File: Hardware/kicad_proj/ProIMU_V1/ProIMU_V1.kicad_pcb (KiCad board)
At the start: 2 copper layers, 50 x 50 mm, 72 parts, among them IC1 MP2731GQC-0000-Z, J1 Conn_01x04, J4 502570-0893, Q1 2SC4213, U1 ADM101E, U2 TJA1051T-3, U3 LTC2942-1, U4 AIR602, U5 BMP280, U6 MPU-9250, U7 TPS54308, U8 TPS54308, U9 STM32F412CEU6

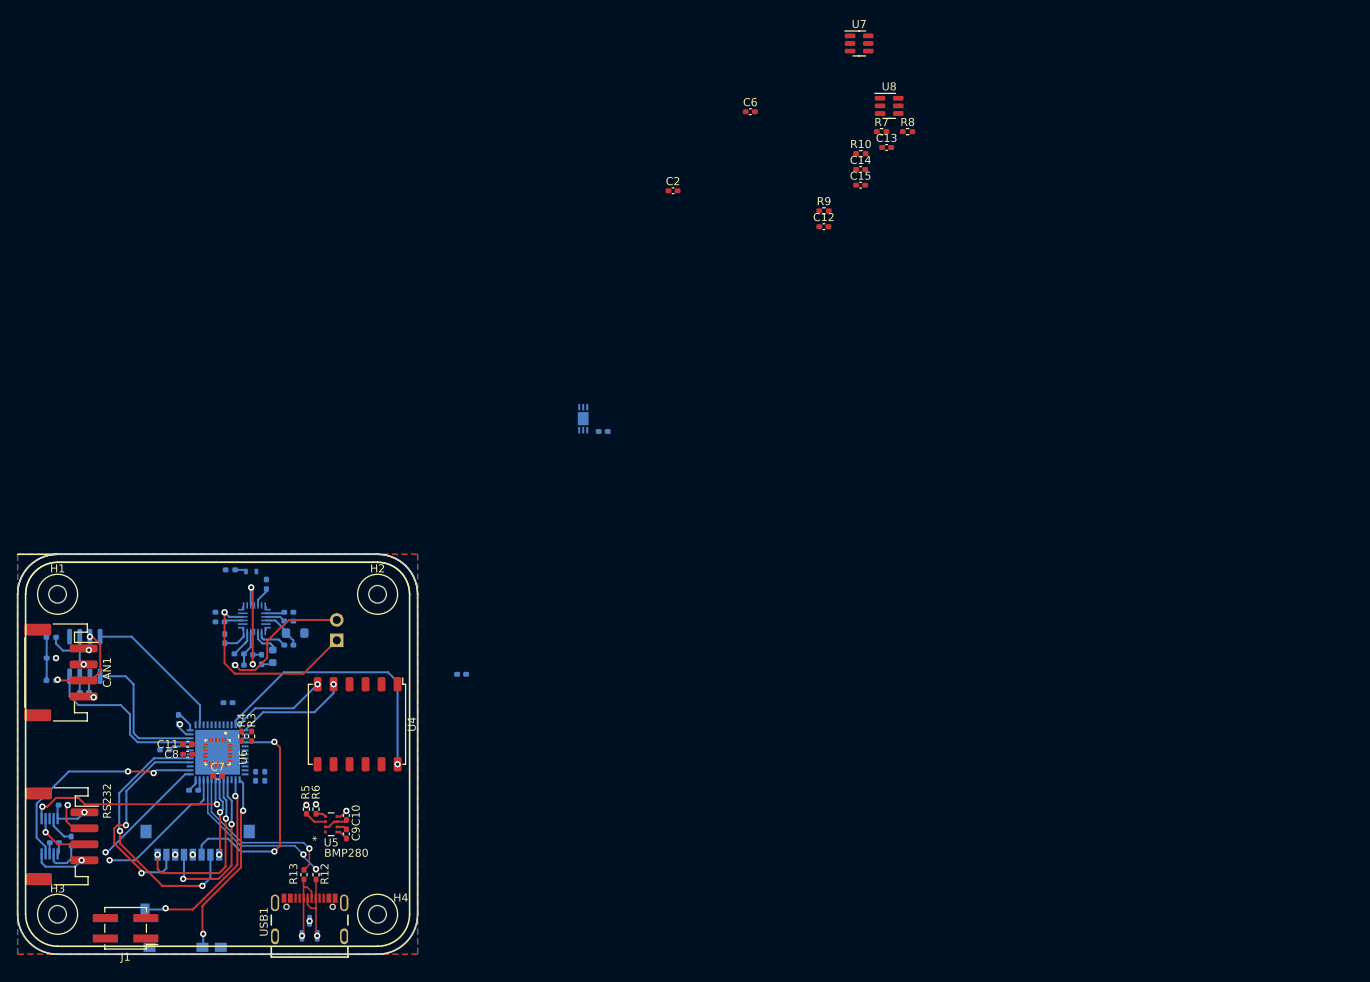
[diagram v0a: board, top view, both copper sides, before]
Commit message: Updated schematic, layout and footprints
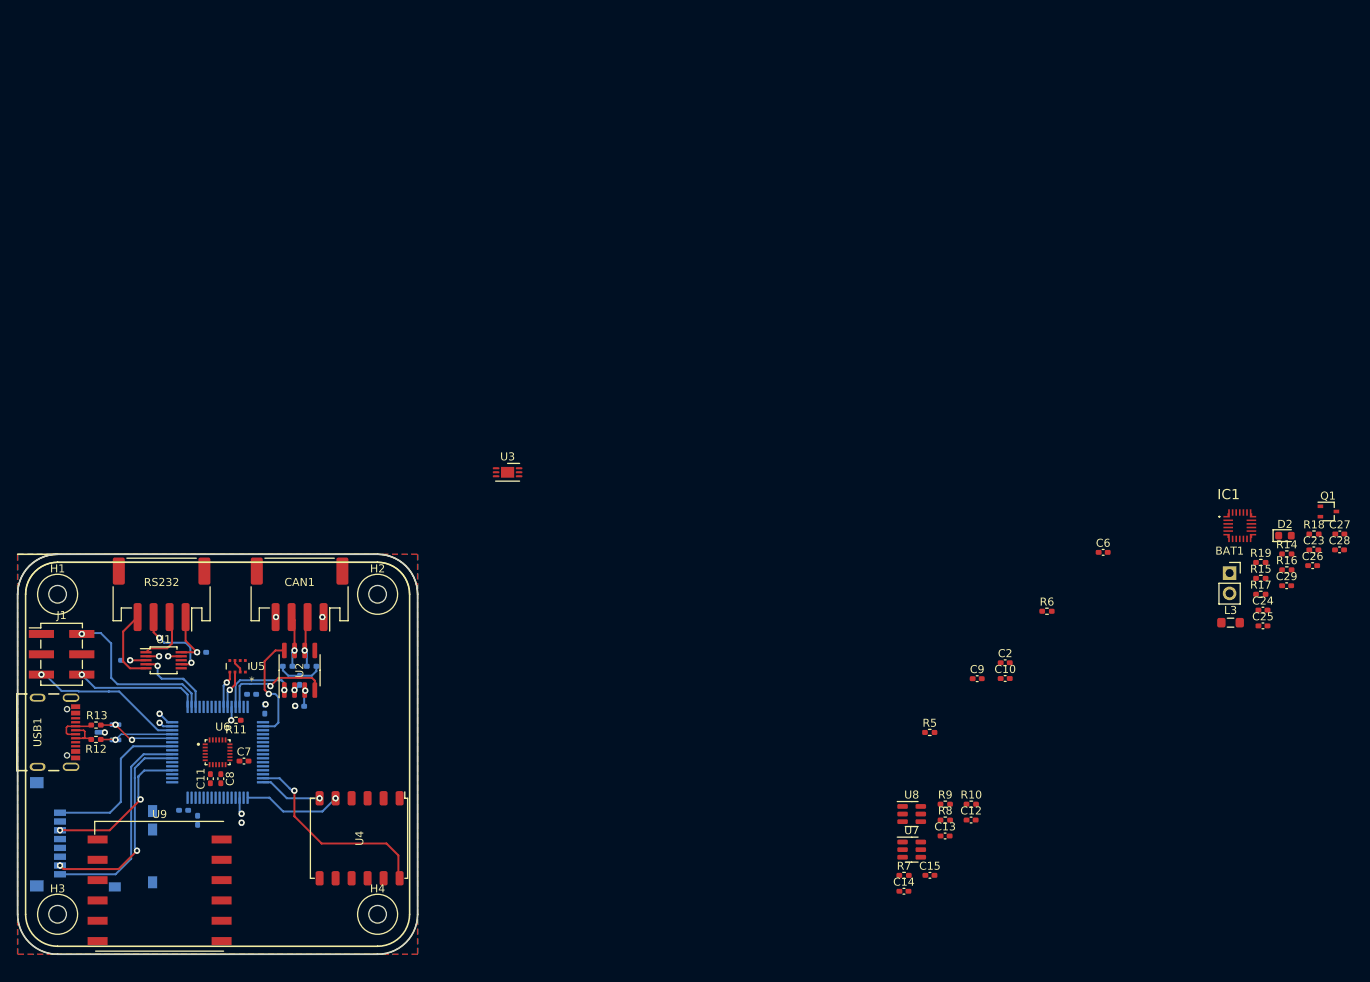
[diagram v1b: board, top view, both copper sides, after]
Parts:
- removed R3, R4: 2.2K, Resistor_SMD:R_0402_1005Metric_Pad0.72x0.64mm_HandSolder
- added U10: STM32F412RETx, Package_QFP:LQFP-64_10x10mm_P0.5mm, B.Cu at (148.5, 105.0)
- BAT1, C23, C24, C25, C26, C27, C28, C29, D2, IC1, L3, Q1, R11, R14, R15, R16, R17, R18, R19, U1, U2, U3: moved to F.Cu
- J1: value Conn_01x04 -> Conn_02x03_Counter_Clockwise; footprint Connector_PinHeader_2.54mm:PinHeader_2x02_P2.54mm_Vertical_SMD -> Connector_PinHeader_2.54mm:PinHeader_2x03_P2.54mm_Vertical_SMD
- U9: value STM32F412CEU6 -> L80-R; footprint footprints:QFN50P700X700X60-49N -> RF_GPS:Quectel_L80-R; moved to F.Cu
- moved C26 136.7 mm to (285.4, 81.7), turned to 0 degrees
- moved R18 135.2 mm to (285.6, 77.7), turned to 0 degrees
- moved Q1 134.9 mm to (287.4, 74.9), turned to 0 degrees
- moved R16 132.1 mm to (282.1, 82.2)
- moved C28 131.9 mm to (288.7, 79.7)
- moved C27 131.8 mm to (288.8, 77.7)
- moved C25 130.4 mm to (279.2, 89.2), turned to 0 degrees
- moved C24 129.8 mm to (279.2, 87.2), turned to 0 degrees
- moved C23 128.4 mm to (285.5, 79.7)
- moved R15 128.2 mm to (278.9, 83.3)
- moved R14 127.6 mm to (282.1, 80.2), turned to 0 degrees
- moved D2 127.4 mm to (281.9, 77.9), turned to 0 degrees
- moved R19 126.6 mm to (278.9, 81.3), turned to 0 degrees
- moved R17 125.2 mm to (278.9, 85.2), turned to 0 degrees
- moved IC1 123.7 mm to (276.3, 76.7), turned to 0 degrees
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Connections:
- net /SCK renamed /MCU/BMP280_I2C1_SDA
- net /SDA renamed /MCU/BMP280_I2C1_SCL
- D1 pad 1: /D1+ -> /Battery/D+
- D1 pad 2: /D1- -> /Battery/D-
- J1 pad 1: /MCU/SWDIO -> /MCU/DEBUG_UART1_RX
- J1 pad 2: /MCU/SWCLK -> /MCU/DEBUG_UART1_TX
- J1 pad 3: /MCU/MCU_RESET -> /MCU/NRST
- J4 pad 1: /MCU/SDCARD_D2 -> /MCU/SDCARD_SDIO_D2
- J4 pad 2: /MCU/SDCARD_D3 -> /MCU/SDCARD_SDIO_D3
- J4 pad 3: /MCU/SDCARD_CMD -> /MCU/SDCARD_SDIO_CLK
- J4 pad 5: /MCU/SDCARD_CLK -> /MCU/SDCARD_SDIO_CMD
- J4 pad 7: /MCU/SDCARD_DO -> /MCU/SDCARD_SDIO_D0
- J4 pad 8: /MCU/SDCARD_D1 -> /MCU/SDCARD_SDIO_D1
- R11 pad 2: Net-(R11-Pad2) -> Net-(U10-Pad60)
- R12 pad 1: /D1+ -> Net-(USB1-PadA6)
- R13 pad 2: /D1- -> Net-(USB1-PadA7)
- U1 pad 4: /MCU/RS232_RX -> /MCU/RS232_UART3_TX
- U1 pad 6: /MCU/RS232_TX -> /MCU/RS232_UART3_RX
- U2 pad 1: /MCU/CAN_TX -> /MCU/CAN1_TX
- U2 pad 4: /MCU/CAN_RX -> /MCU/CAN1_RX
- U4 pad 5: /MCU/WIFI_UART2_TX -> /MCU/WIFI_UART2_RX
- U4 pad 6: /MCU/WIFI_UART2_RX -> /MCU/WIFI_UART2_TX
- U6 pad 12: /MCU/MPU9250_INT -> /MCU/MPU9250_INT_EXTI4
- U6 pad 22: +3V3 -> /MCU/MPU9250_SPI1_nCSS
- U6 pad 23: /MPU9250_SDA -> /MCU/MPU9250_SPI1_SCK
- U6 pad 24: /MPU9250_SCK -> /MCU/MPU9250_SPI1_MISO
- U6 pad 9: unconnected-(U6-Pad9) -> /MCU/MPU9250_SPI1_MOSI
- U9 pad 1: +BATT -> unconnected-(U9-Pad1)
- U9 pad 10: /MCU/MPU9250_INT -> unconnected-(U9-Pad10)
- U9 pad 11: /MCU/WIFI_RESET -> unconnected-(U9-Pad11)
- U9 pad 12: /MCU/WIFI_UART2_RX -> Net-(U9-Pad12)
- U9 pad 2: /MCU/CAN_SHUTDOWN -> unconnected-(U9-Pad2)
- U9 pad 3: unconnected-(U9-Pad3) -> Net-(U9-Pad12)
- U9 pad 7: /MCU/MCU_RESET -> unconnected-(U9-Pad7)
- U9 pad 8: GND -> unconnected-(U9-Pad8)
- U9 pad 9: +3V3 -> unconnected-(U9-Pad9)
- USB1 pad A6: /D1+ -> Net-(USB1-PadA6)
- USB1 pad A7: /D1- -> Net-(USB1-PadA7)
- USB1 pad B6: /D1+ -> Net-(USB1-PadA6)
- USB1 pad B7: /D1- -> Net-(USB1-PadA7)
- USB1 pad S1: Earth -> unconnected-(USB1-PadS1)
- USB1 pad S2: Earth -> unconnected-(USB1-PadS2)
- USB1 pad S3: Earth -> unconnected-(USB1-PadS3)
- USB1 pad S4: Earth -> unconnected-(USB1-PadS4)
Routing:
- net /MCU/SDCARD_D3: track 33.8 -> 0.00 mm, vias 2 -> 0
- net /MCU/SDCARD_CMD: track 29.3 -> 0.00 mm, vias 2 -> 0
- net /MCU/RS232_RX: track 27.8 -> 0.00 mm, vias 2 -> 0
- net /MCU/SDCARD_DO: track 27.5 -> 0.00 mm, vias 2 -> 0
- net /MCU/RS232_TX: track 27.3 -> 0.00 mm, vias 2 -> 0
- net /MCU/SDCARD_SDIO_D1: track 0.00 -> 27.0 mm
- net /MCU/SDCARD_SDIO_D0: track 0.00 -> 26.4 mm, vias 0 -> 2
- net Net-(BAT1-Pad1): track 25.2 -> 0.00 mm, vias 1 -> 0
- net /MCU/SDCARD_DET_LEVEL: track 24.8 -> 0.00 mm, vias 2 -> 0
- net /MCU/SDCARD_DET_SWT: track 23.3 -> 0.00 mm, vias 2 -> 0
- net /MCU/SDCARD_D1: track 21.9 -> 0.00 mm, vias 2 -> 0
- net /MCU/CAN_RX: track 21.4 -> 0.00 mm
- net /MCU/DEBUG_UART1_TX: track 0.00 -> 21.1 mm, vias 0 -> 1
- net /MCU/SDCARD_CLK: track 20.8 -> 0.00 mm, vias 2 -> 0
- net /MCU/SDCARD_SDIO_D2: track 0.00 -> 20.6 mm
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
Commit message: Updated Layout
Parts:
- BAT1, C2, C23, C24, C25, C26, C27, C28, C29, D2, IC1, L3, Q1, R14, R15, R16, R17, R18, R19, U3: moved to B.Cu
- moved Q1 149.2 mm to (156.9, 147.3)
- moved C28 143.4 mm to (159.4, 141.6), turned to -90 degrees
- moved R16 143.3 mm to (154.6, 147.5), turned to 90 degrees
- moved C27 142.0 mm to (162.3, 142.2), turned to -90 degrees
- moved R18 141.3 mm to (157.4, 137.1)
- moved C26 141.1 mm to (156.5, 139.1), turned to -90 degrees
- moved D2 139.9 mm to (157.2, 141.3), turned to 180 degrees
- moved BAT1 138.6 mm to (148.7, 139.7)
- moved C29 138.6 mm to (154.6, 138.4)
- moved C23 137.2 mm to (163.4, 142.2), turned to -90 degrees
- moved R19 136.3 mm to (157.9, 143.9), turned to 180 degrees
- moved R17 135.8 mm to (156.2, 143.3), turned to -90 degrees
- moved R15 135.5 mm to (154.6, 137.1)
- moved C25 133.1 mm to (159.9, 148.1)
- moved IC1 130.0 mm to (161.9, 138.4), turned to 90 degrees
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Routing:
- net VDD: track 0.00 -> 10.0 mm, vias 0 -> 1
- net Net-(BAT1-Pad1): track 0.00 -> 8.39 mm, vias 0 -> 2
- net GND: track 3.61 -> 9.29 mm, vias 8 -> 18
- net Net-(IC1-Pad11): track 0.00 -> 5.40 mm
- net Net-(BAT1-Pad2): track 0.00 -> 5.32 mm, vias 0 -> 1
- net Net-(D2-Pad1): track 0.00 -> 4.03 mm
- net Net-(IC1-Pad22): track 0.00 -> 3.65 mm, vias 0 -> 1
- net Net-(C28-Pad1): track 0.00 -> 2.69 mm
- net Net-(IC1-Pad12): track 0.00 -> 2.42 mm
- net Net-(C28-Pad2): track 0.00 -> 2.37 mm
- net Net-(IC1-Pad24): track 0.00 -> 2.27 mm
- net /Battery/SYSTEM_OUT: track 0.00 -> 2.04 mm
- net Net-(C24-Pad1): track 0.00 -> 1.94 mm
- net Net-(C27-Pad1): track 0.00 -> 1.85 mm
- net Net-(Q1-Pad1): track 0.00 -> 1.73 mm
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
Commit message: Updated Layout
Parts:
- C6: moved to B.Cu
- moved C6 138.3 mm to (126.0, 117.1), turned to 90 degrees
- moved U4 8.45 mm to (166.2, 107.3)
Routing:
- net /MCU/NRST: track 0.00 -> 32.5 mm, vias 0 -> 1
- net /MCU/SDCARD_SDIO_CMD: track 0.00 -> 32.2 mm, vias 0 -> 2
- net /MCU/SDCARD_SDIO_D3: track 0.00 -> 27.7 mm, vias 0 -> 2
- net /MCU/DEBUG_UART1_RX: track 0.00 -> 26.9 mm, vias 0 -> 3
- net /MCU/SDCARD_DET_LEVEL: track 0.00 -> 22.4 mm
- net /MCU/SDCARD_DET_SWT: track 0.00 -> 12.7 mm, vias 0 -> 2
- net /MCU/WIFI_RESET: track 25.7 -> 18.8 mm
- net /MCU/WIFI_UART2_RX: track 12.4 -> 19.2 mm
- net /MCU/WIFI_UART2_TX: track 7.90 -> 14.3 mm
- net GND: track 9.29 -> 12.4 mm, vias 18 -> 21
- net +3V3: track 7.20 -> 10.3 mm, vias 2 -> 3
- net /MCU/SDCARD_SDIO_CLK: track 19.2 -> 21.4 mm
- net /MCU/SDCARD_SDIO_D2: track 20.6 -> 19.8 mm

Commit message: Updated Layout
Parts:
- moved C25 33.2 mm to (152.7, 115.7), turned to 180 degrees
- moved R16 31.4 mm to (158.0, 116.3), turned to -90 degrees
- moved Q1 30.8 mm to (155.7, 116.5), turned to 180 degrees
- moved L3 28.0 mm to (152.5, 118.4), turned to -90 degrees
- moved C23 25.0 mm to (149.2, 121.6), turned to 90 degrees
- moved R14 24.5 mm to (146.2, 124.9), turned to 0 degrees
- moved R19 24.2 mm to (154.7, 119.9), turned to 0 degrees
- moved C27 23.8 mm to (150.3, 121.6), turned to 90 degrees
- moved R17 22.8 mm to (156.4, 120.5), turned to 90 degrees
- moved BAT1 21.8 mm to (163.9, 124.0), turned to 180 degrees
- moved C28 20.3 mm to (153.2, 122.2), turned to 90 degrees
- moved D2 18.9 mm to (155.4, 122.5), turned to 0 degrees
- moved U3 17.7 mm to (159.1, 123.5), turned to 0 degrees
- moved IC1 17.1 mm to (150.7, 125.4), turned to -90 degrees
- moved C26 14.4 mm to (156.1, 124.7), turned to 90 degrees
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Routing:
- net /MCU/MPU9250_INT_EXTI4: track 0.00 -> 13.0 mm, vias 0 -> 1
- net /MCU/MPU9250_SPI1_MISO: track 0.00 -> 10.5 mm, vias 0 -> 1
- net /MCU/MPU9250_SPI1_MOSI: track 0.00 -> 8.97 mm, vias 0 -> 1
- net /MCU/MPU9250_SPI1_nCSS: track 0.00 -> 8.23 mm, vias 0 -> 1
- net /MCU/MPU9250_SPI1_SCK: track 0.00 -> 8.19 mm, vias 0 -> 1
- net GND: track 12.4 -> 19.3 mm
- net +3V3: track 10.3 -> 11.6 mm
- net Net-(C8-Pad1): track 0.00 -> 1.27 mm
- net +5V: track 3.57 -> 4.80 mm
- net /MCU/NRST: track 32.5 -> 33.7 mm

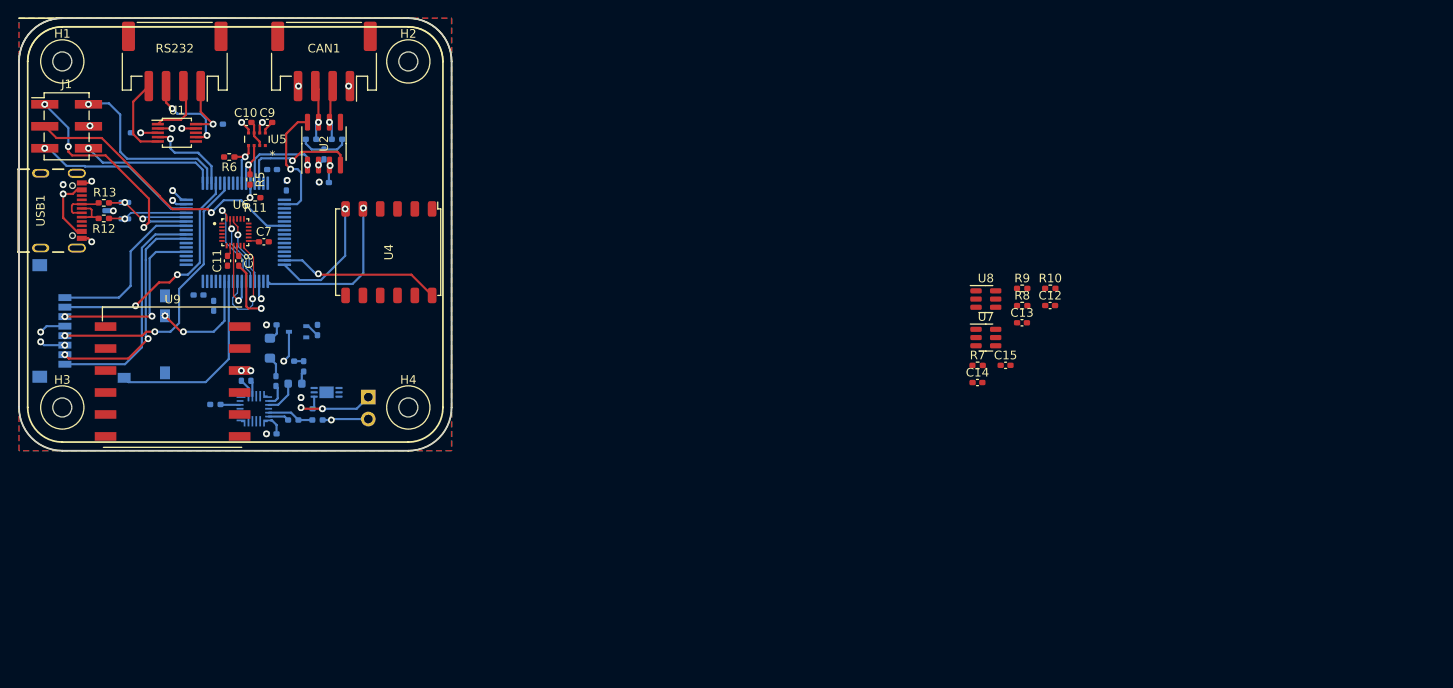
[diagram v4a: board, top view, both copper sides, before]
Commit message: Updated Layout, schematic, added new symbol and footprint
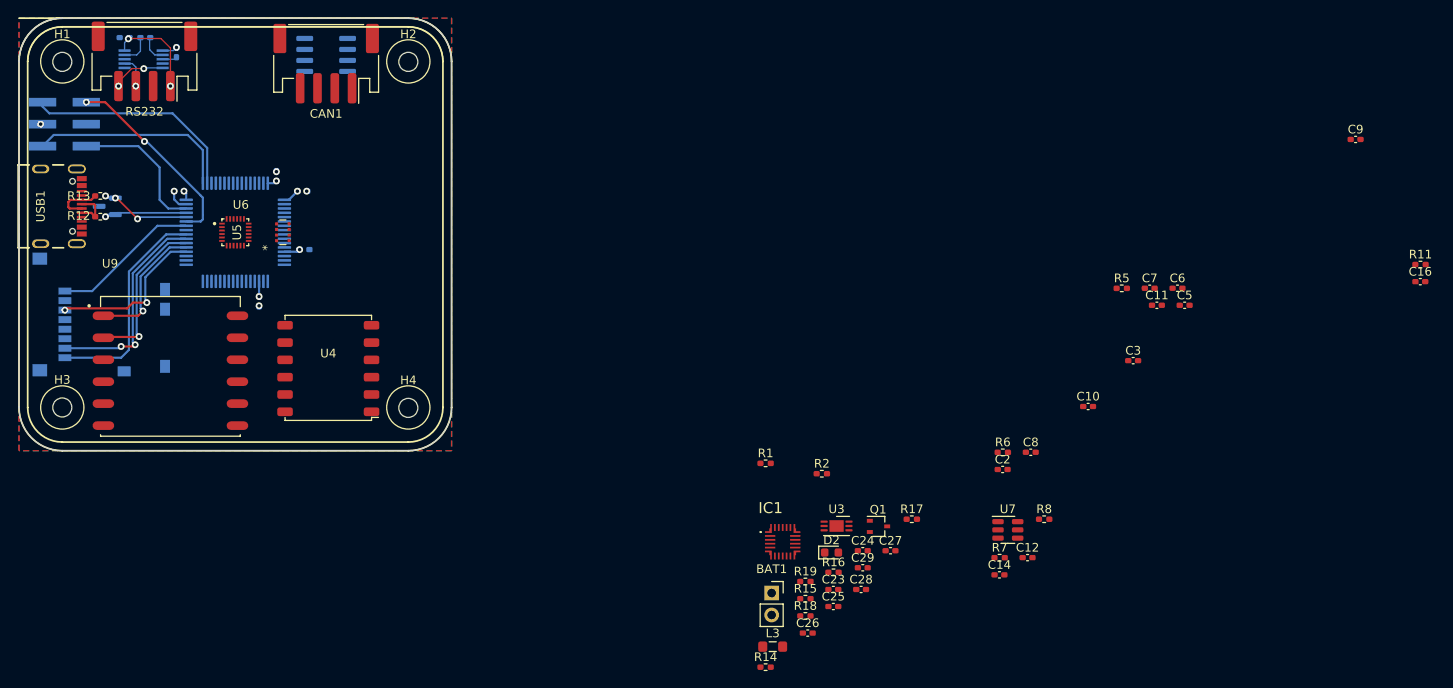
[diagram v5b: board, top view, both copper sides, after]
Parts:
- removed C13, C15: 1uF, Capacitor_SMD:C_0402_1005Metric_Pad0.74x0.62mm_HandSolder
- removed R10, R9: 10K, Resistor_SMD:R_0402_1005Metric_Pad0.72x0.64mm_HandSolder
- removed U8: TPS54308, Package_TO_SOT_SMD:SOT-23-6
- BAT1, C16, C2, C23, C24, C25, C26, C27, C28, C29, C3, C5, C6, D2, IC1, L3, Q1, R1, R14, R15, R16, R17, R18, R19, R2, U3: moved to F.Cu
- J1, U1, U2: moved to B.Cu
- U9: value L80-R -> L80-M39; footprint RF_GPS:Quectel_L80-R -> footprints:XCVR_L80-M39
- moved C16 139.5 mm to (285.5, 110.7), turned to 0 degrees
- moved R11 134.9 mm to (285.5, 108.7), turned to 0 degrees
- moved C6 131.5 mm to (257.4, 111.5), turned to 0 degrees
- moved C9 125.8 mm to (278.0, 94.3), turned to 0 degrees
- moved C2 113.3 mm to (237.2, 132.4), turned to 0 degrees
- moved C11 107.6 mm to (255.0, 113.4), turned to 0 degrees
- moved C10 102.7 mm to (247.1, 125.1), turned to 0 degrees
- moved C7 102.5 mm to (254.2, 111.5)
- moved R5 101.6 mm to (251.0, 111.5), turned to 0 degrees
- moved C5 101.0 mm to (258.2, 113.4), turned to 0 degrees
- moved C3 95.8 mm to (252.3, 119.8)
- moved R6 95.7 mm to (237.2, 130.4), turned to 0 degrees
- moved C8 94.2 mm to (240.4, 130.4), turned to 0 degrees
- moved C27 76.7 mm to (224.2, 141.8), turned to 0 degrees
- moved C23 72.7 mm to (217.6, 146.3), turned to 0 degrees
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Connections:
- U10 pad 11: unconnected-(U10-Pad11) -> /MCU/GPS_RESET
- U10 pad 37: /MCU/GNSS_UART6_TX -> /MCU/GPS_UART6_TX
- U10 pad 38: /MCU/GNSS_UART6_RX -> /MCU/GPS_UART6_RX
- U9 pad 1: unconnected-(U9-Pad1) -> /MCU/GPS_UART6_TX
- U9 pad 10: unconnected-(U9-Pad10) -> /MCU/GPS_RESET
- U9 pad 12: Net-(U9-Pad12) -> GND
- U9 pad 2: unconnected-(U9-Pad2) -> /MCU/GPS_UART6_RX
- U9 pad 3: Net-(U9-Pad12) -> GND
- U9 pad 4: unconnected-(U9-Pad4) -> +3V3
- U9 pad 5: unconnected-(U9-Pad5) -> +3V3
- U9 pad 9: unconnected-(U9-Pad9) -> (no net)
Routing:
- net /MCU/NRST: track 33.7 -> 0.00 mm, vias 1 -> 0
- net /MCU/SDCARD_SDIO_CMD: track 32.2 -> 0.00 mm, vias 2 -> 0
- net /MCU/SDCARD_SDIO_D3: track 27.7 -> 0.00 mm, vias 2 -> 0
- net /MCU/SDCARD_DET_LEVEL: track 22.4 -> 0.00 mm
- net /MCU/WIFI_UART2_RX: track 19.2 -> 0.00 mm, vias 1 -> 0
- net /MCU/WIFI_RESET: track 18.8 -> 0.00 mm, vias 1 -> 0
- net /MCU/GPS_UART6_RX: track 0.00 -> 18.7 mm, vias 0 -> 1
- net GND: track 19.3 -> 3.00 mm, vias 21 -> 5
- net /MCU/GPS_UART6_TX: track 0.00 -> 15.6 mm, vias 0 -> 1
- net /MCU/WIFI_UART2_TX: track 14.3 -> 0.00 mm, vias 1 -> 0
- net /MCU/CAN_SHUTDOWN: track 14.0 -> 0.00 mm, vias 1 -> 0
- net /MCU/CAN1_RX: track 14.0 -> 0.00 mm, vias 1 -> 0
- net /MCU/MPU9250_INT_EXTI4: track 13.0 -> 0.00 mm, vias 1 -> 0
- net /MCU/SDCARD_DET_SWT: track 12.7 -> 0.00 mm, vias 2 -> 0
- net /MCU/MPU9250_SPI1_MISO: track 10.5 -> 0.00 mm, vias 1 -> 0
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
